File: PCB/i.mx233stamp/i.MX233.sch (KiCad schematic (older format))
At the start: 83 parts, among them IC1 iMX233, J1 MICROSD, J2 POWER_5V, P1 CONN_12X2, P2 CONN_12X2, P3 CONN_1, P4 CONN_4X2, P5 CONN_1, P6 CONN_2, Q1 MMDT3904, SW3 RESET, U1 ADM3101E, X1 24MHz

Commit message: Eliminación de los errores encontrados por el DRC
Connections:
- wire segments 370 -> 374
- no-connect marks 9 -> 8

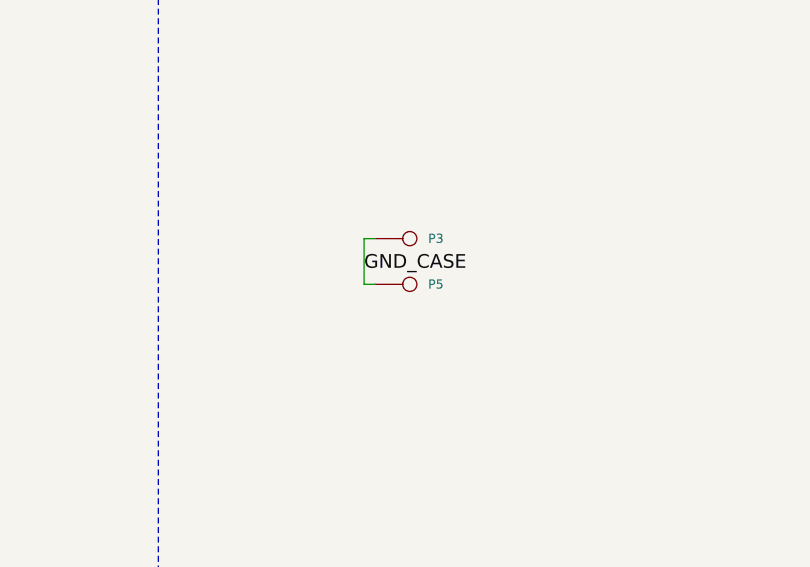
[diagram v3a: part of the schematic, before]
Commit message: ubicación de los labels en las capas de silkscreen, ubicación de los diodos de proteccción contra estática de los puertos USB
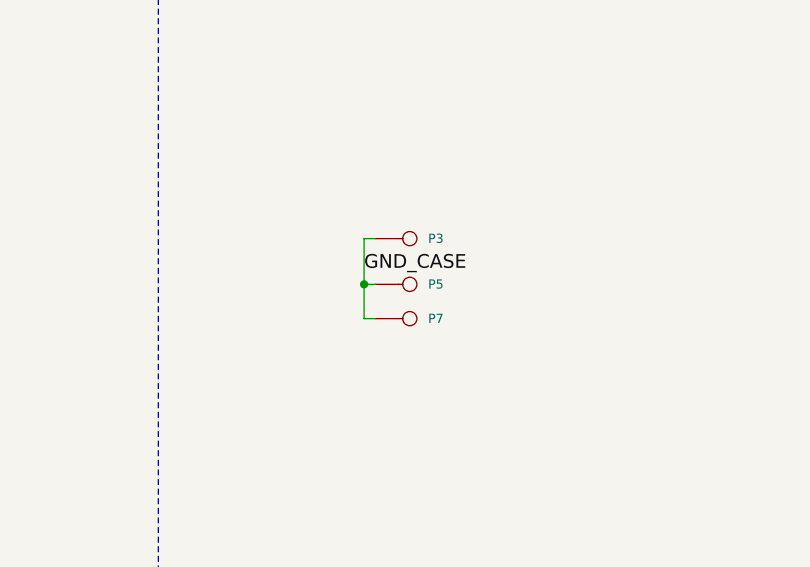
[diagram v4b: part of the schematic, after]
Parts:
- added P7: CONN_1, MHOLE, symbol CONN_1
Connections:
- wire segments 374 -> 375
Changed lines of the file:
@@
-EESchema Schematic File Version 2  date Tue 16 Aug 2011 06:52:22 AM COT
+EESchema Schematic File Version 2  date Wed 17 Aug 2011 08:52:32 AM COT
 LIBS:con-jack
 LIBS:adm3101e
@@
 Sheet 4 4
 Title ""
-Date "16 aug 2011"
+Date "17 aug 2011"
 Rev ""
 Comp ""
@@
 	11525 1100 11425 1100
 Wire Wire Line
-	12250 9150 12200 9150
-Wire Wire Line
-	12200 9150 12200 8950
-Wire Wire Line
-	12200 8950 12250 8950
+	12200 9150 12250 9150
+Wire Wire Line
+	12250 8950 12200 8950
 Wire Wire Line
 	900  1850 900  1800
@@
 Wire Wire Line
 	10625 1300 10525 1300
+Wire Wire Line
+	12250 9300 12200 9300
+Wire Wire Line
+	12200 9300 12200 8950
+Connection ~ 12200 9150
+$Comp
+L CONN_1 P7
+U 1 1 4E4BC769
+P 12400 9300
+F 0 "P7" H 12480 9300 40  0000 L CNN
+F 1 "CONN_1" H 12400 9355 30  0001 C CNN
+F 2 "MHOLE" H 12400 9300 60  0001 C CNN
+	1    12400 9300
+	1    0    0    -1
+$EndComp
 $Comp
 L GND #PWR041

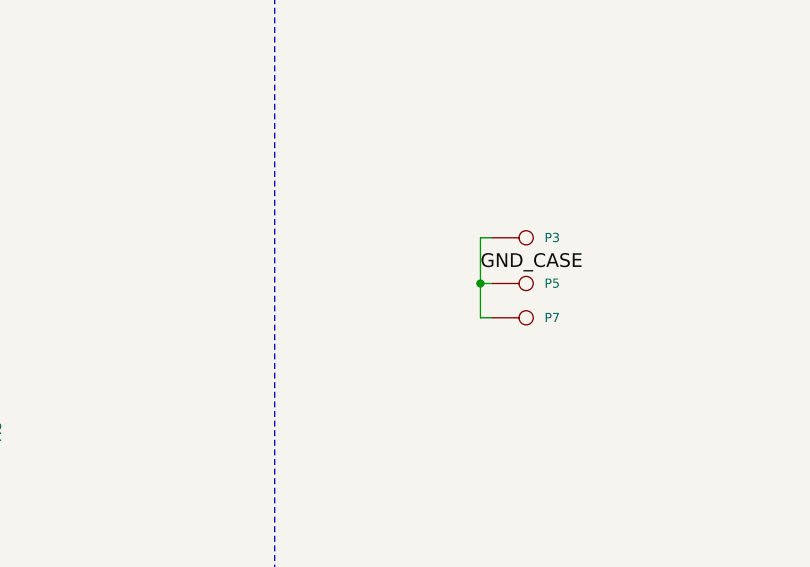
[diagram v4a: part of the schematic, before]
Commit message: LED0603 footprint has been fixed
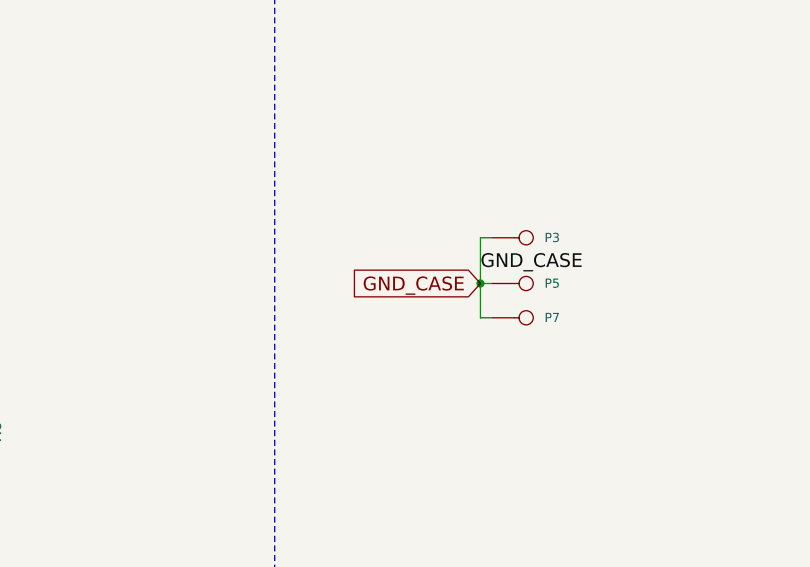
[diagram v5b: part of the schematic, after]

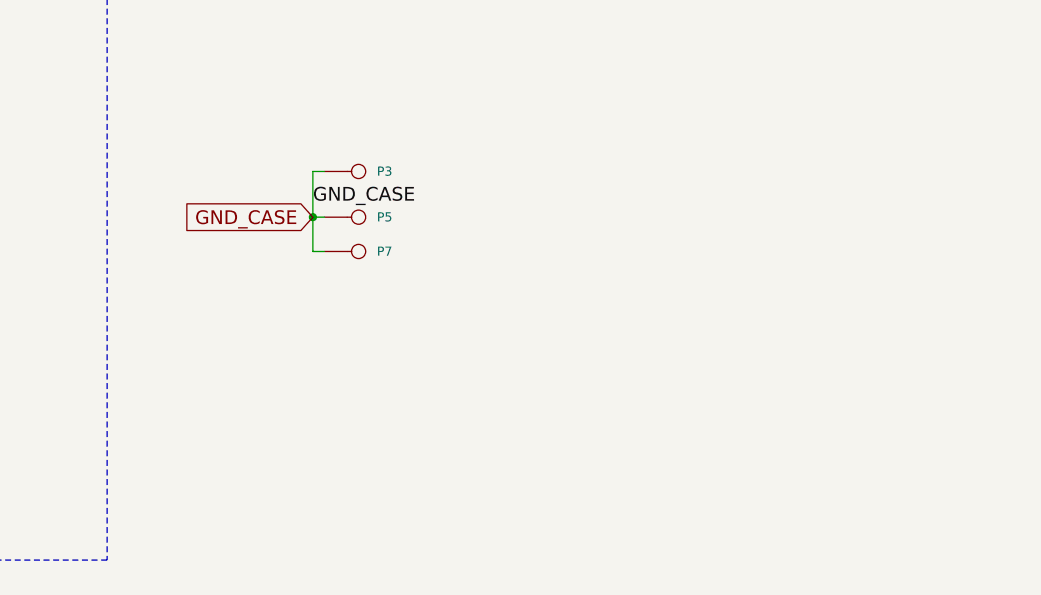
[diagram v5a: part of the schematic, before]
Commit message: Finalización del ruteo de la red GND_case, conexión de esta red con la tierra del circuito, limpeza y depuración
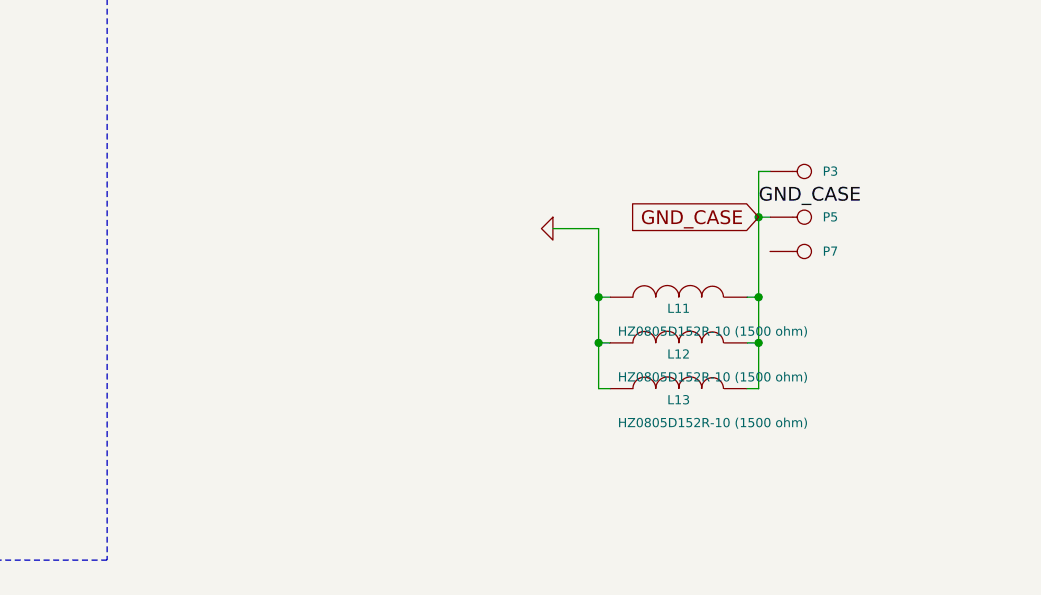
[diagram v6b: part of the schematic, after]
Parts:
- added L11, L12, L13: HZ0805D152R-10 (1500 ohm), SM0805, symbol INDUCTOR
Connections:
- wire segments 375 -> 382
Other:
- moved on the sheet: P3, P5, P7

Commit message: fix
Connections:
- wire segments 382 -> 383
